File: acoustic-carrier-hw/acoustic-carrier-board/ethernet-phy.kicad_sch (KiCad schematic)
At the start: 52 parts, among them IC1 ECP5-BGA256, J12 HR911130A, U1 KSZ9031RN, Y1 25MHz

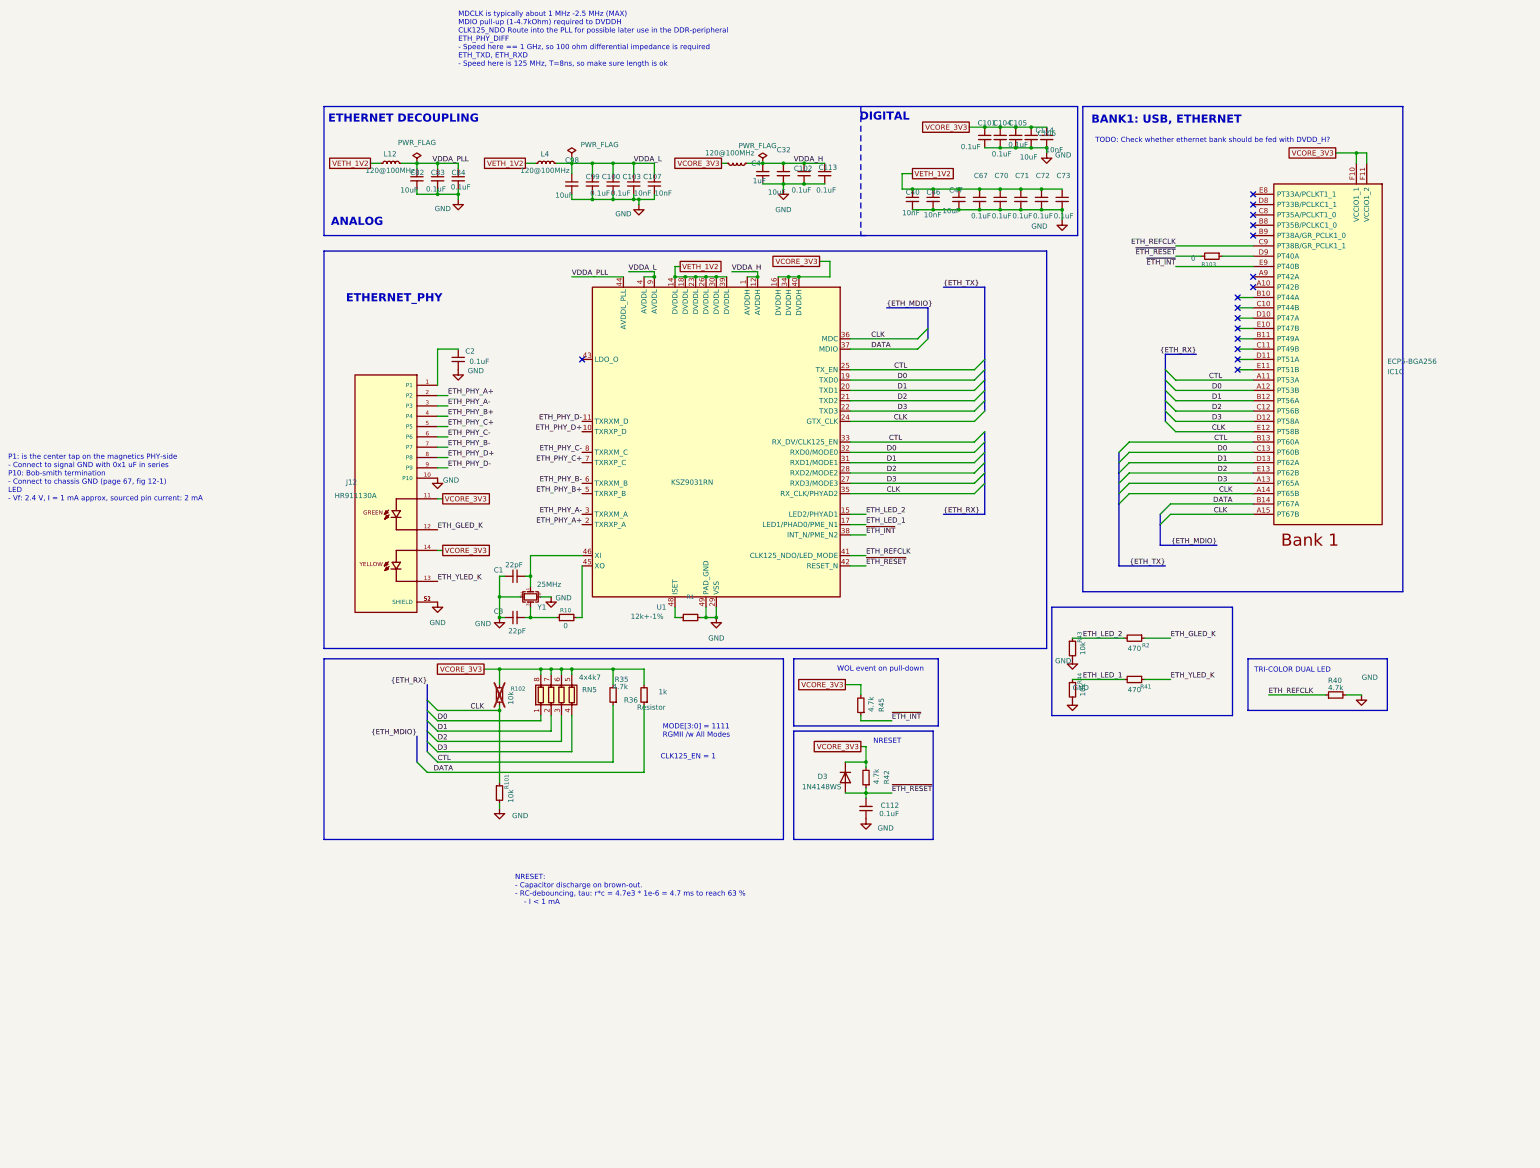
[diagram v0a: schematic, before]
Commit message: [carrier] Added hierarchical labels
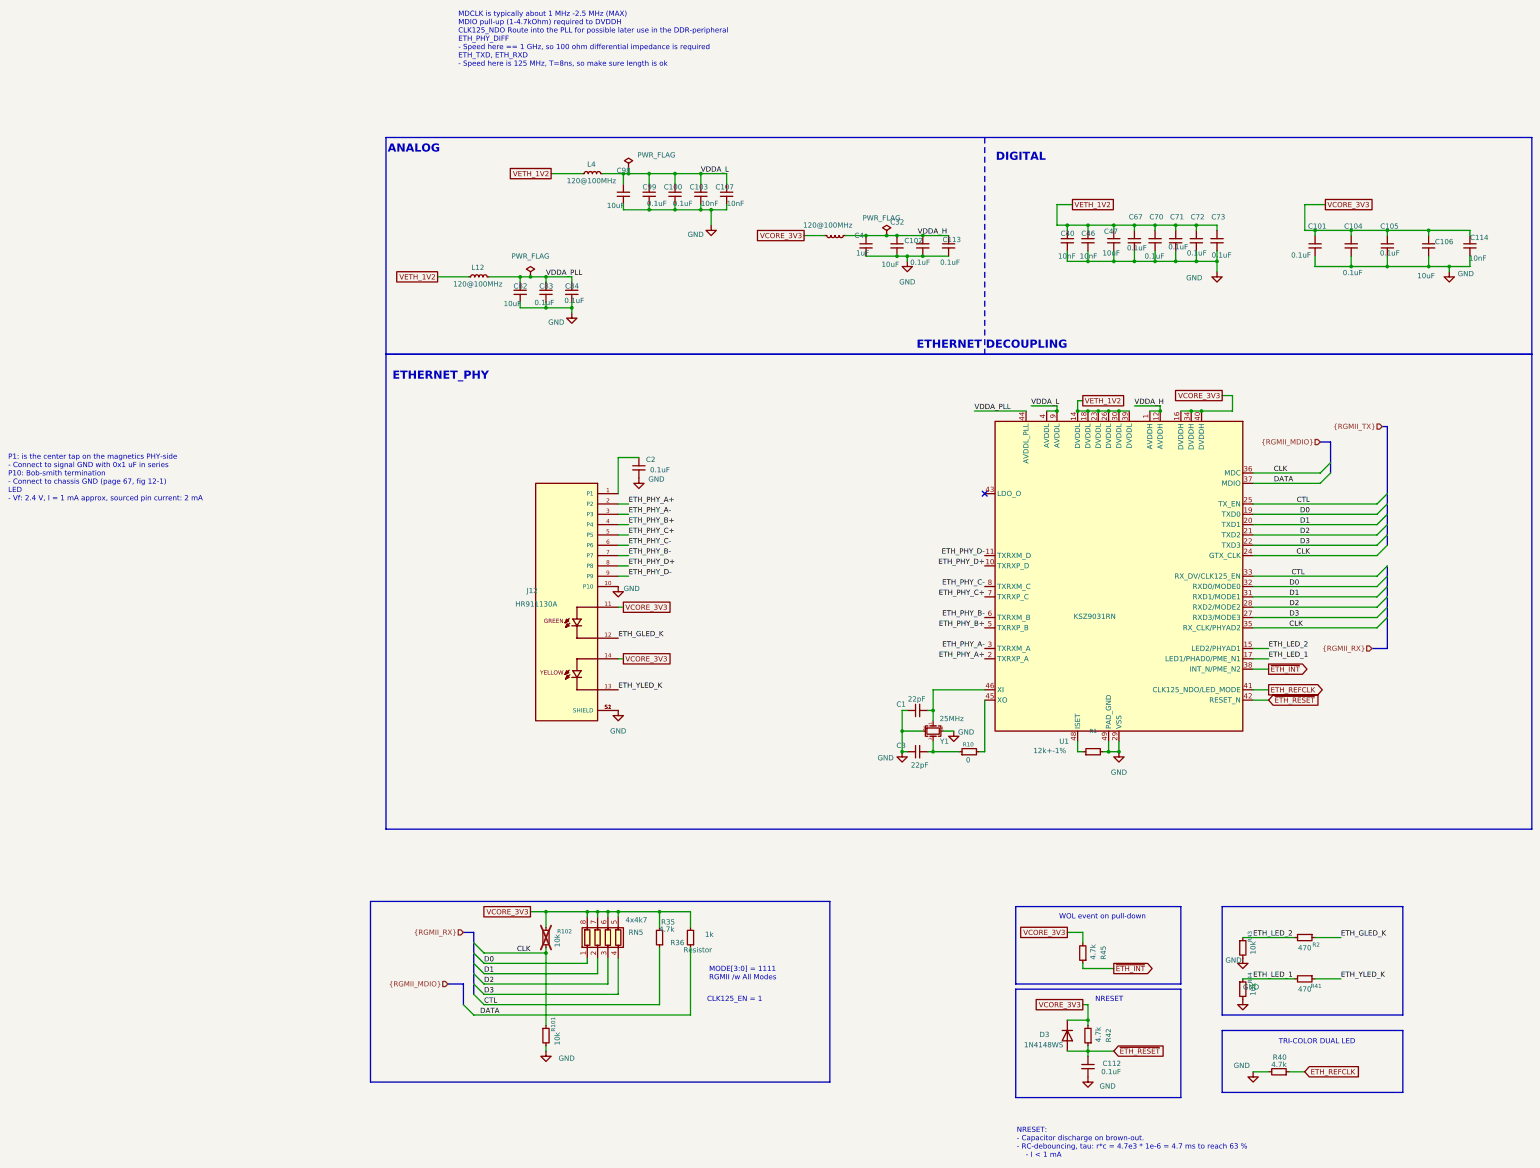
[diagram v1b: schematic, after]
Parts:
- removed IC1: ECP5-BGA256, iw-fpga_mcu:BGA256C80P16X16_1400X1400X170, symbol iw-fpga_mcu:ECP5-BGA256
- removed R103: 0, Resistor_SMD:R_0603_1608Metric, symbol Device:R_Small
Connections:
- no-connect marks 16 -> 1
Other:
- note removed: "BANK1: USB, ETHERNET"
- note removed: "TODO: Check whether ethernet bank should be fed with DVDD_H?"
- moved on the sheet: C1, C100, C101, C102, C103, C104, C105, C106, C107, C112, C113, C114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

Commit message: [¢arrier] Did major cchecks of ETH, DDR, ANALOG, config (next) check buffer circuit driven by USB-CC, then start layout
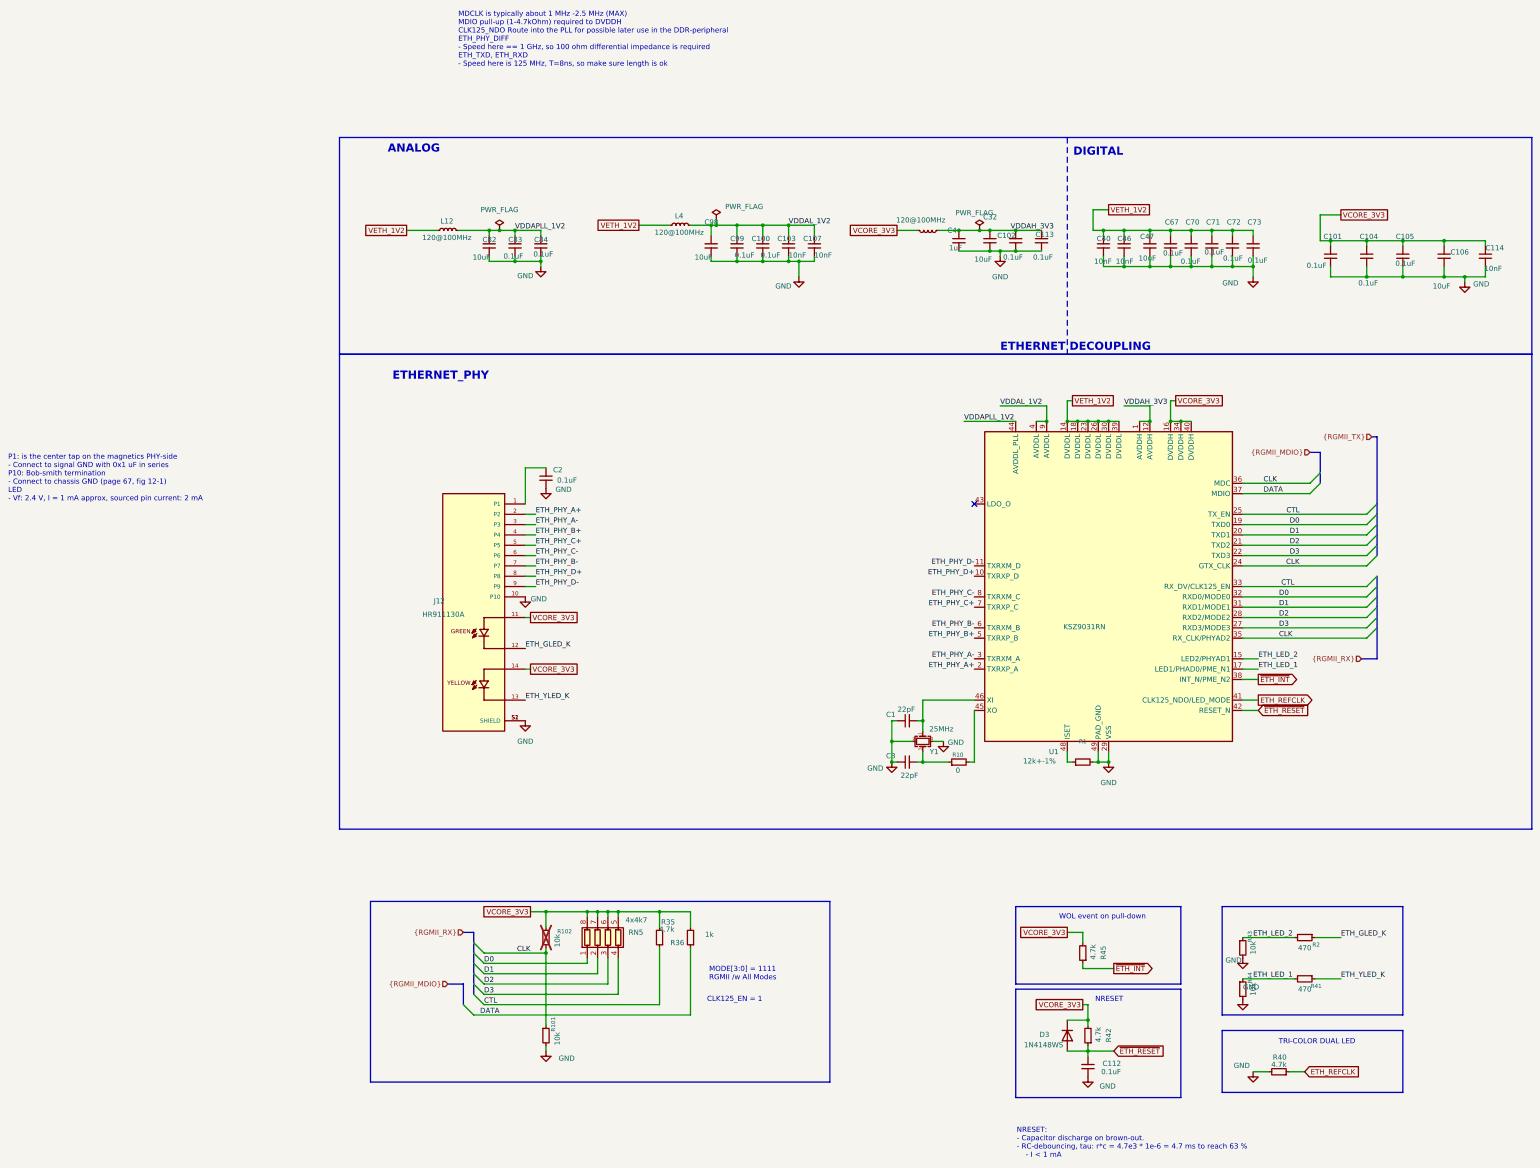
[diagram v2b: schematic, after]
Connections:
- net VDDA_H renamed VDDAH_3V3
- net VDDA_L renamed VDDAL_1V2
- net VDDA_PLL renamed VDDAPLL_1V2
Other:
- moved on the sheet: C1, C100, C101, C102, C103, C104, C105, C106, C107, C113, C114, C2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

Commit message: [carrier] Added testpoints
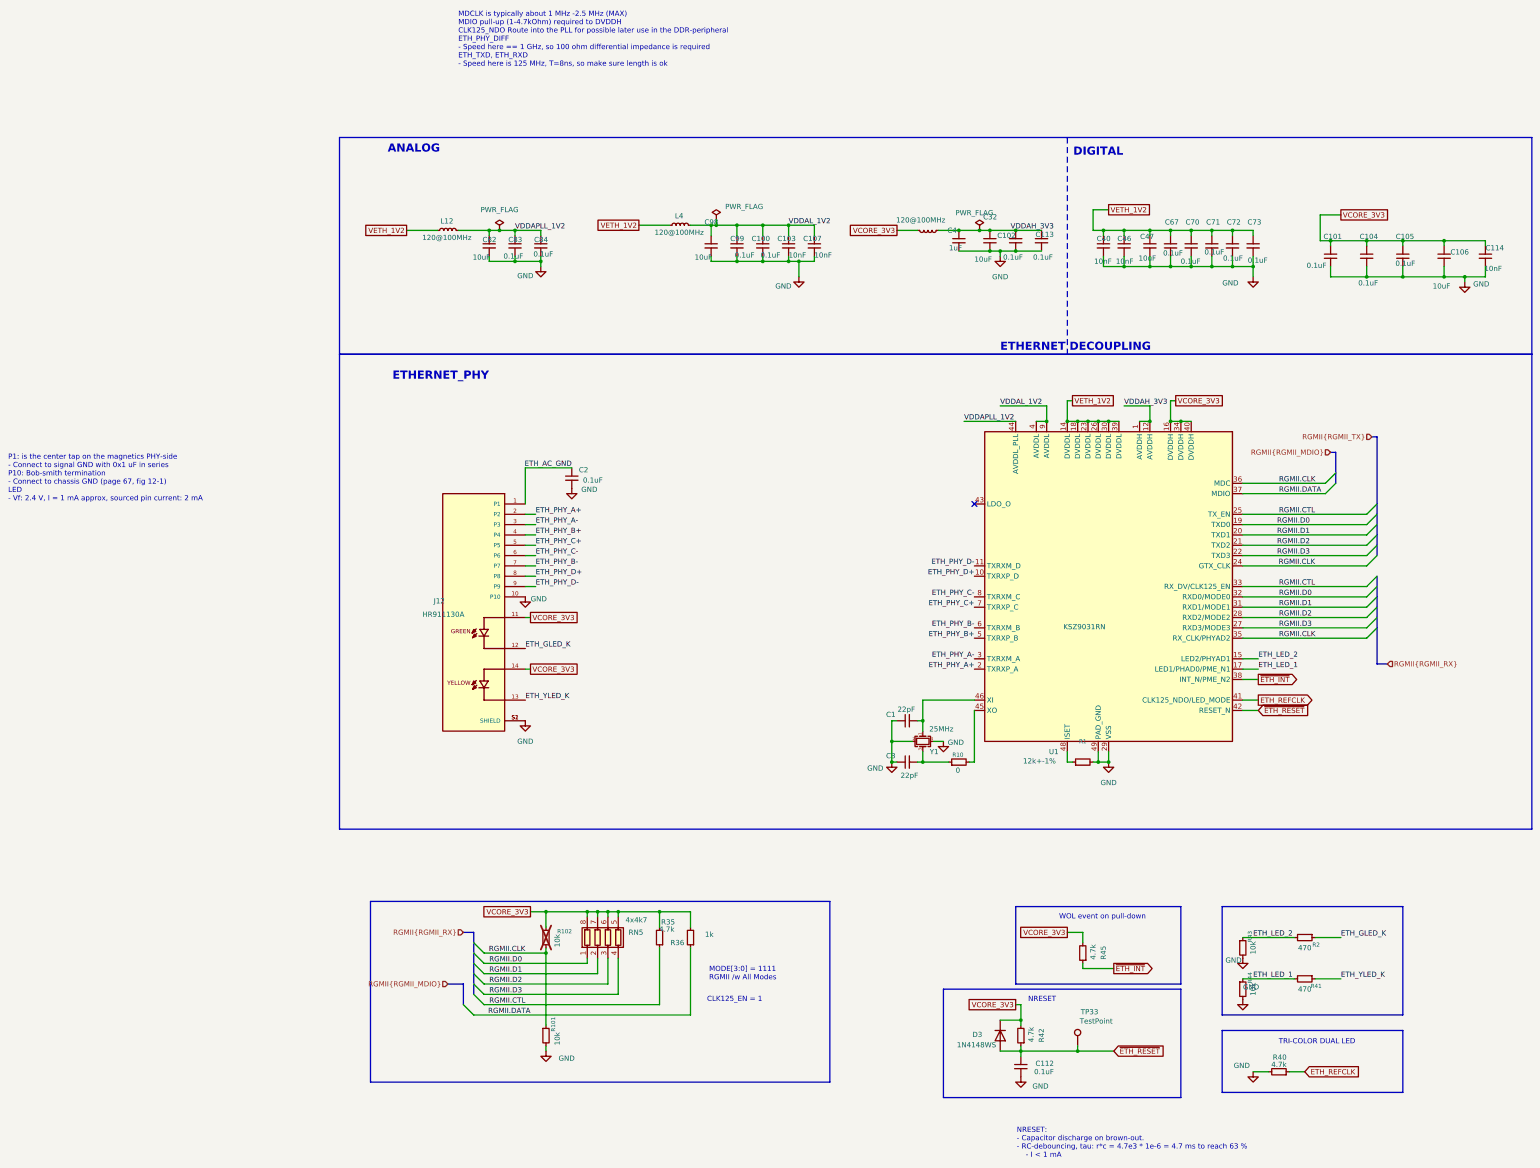
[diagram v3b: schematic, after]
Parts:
- added TP33: TestPoint, TestPoint:TestPoint_Loop_D1.80mm_Drill1.0mm_Beaded, symbol Connector:TestPoint
- R35, R40, R42, R45: LPN 0402WGF4701TCE -> C25900; MPN C25900 -> 0402WGF4701TCE
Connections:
- net ~{ETH_RESET}: now also TP33.1
- net ETH_AC_GND: now reaches C2.1, J12.1 (P1)
- net CLK renamed RGMII.CLK
- net CTL renamed RGMII.CTL
- net D0 renamed RGMII.D0
- net D1 renamed RGMII.D1
- net D2 renamed RGMII.D2
- net D3 renamed RGMII.D3
- net DATA renamed RGMII.DATA
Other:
- moved on the sheet: C112, C2, D3, R42

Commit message: [carrier] Finished rough layout, p (put together according to component category
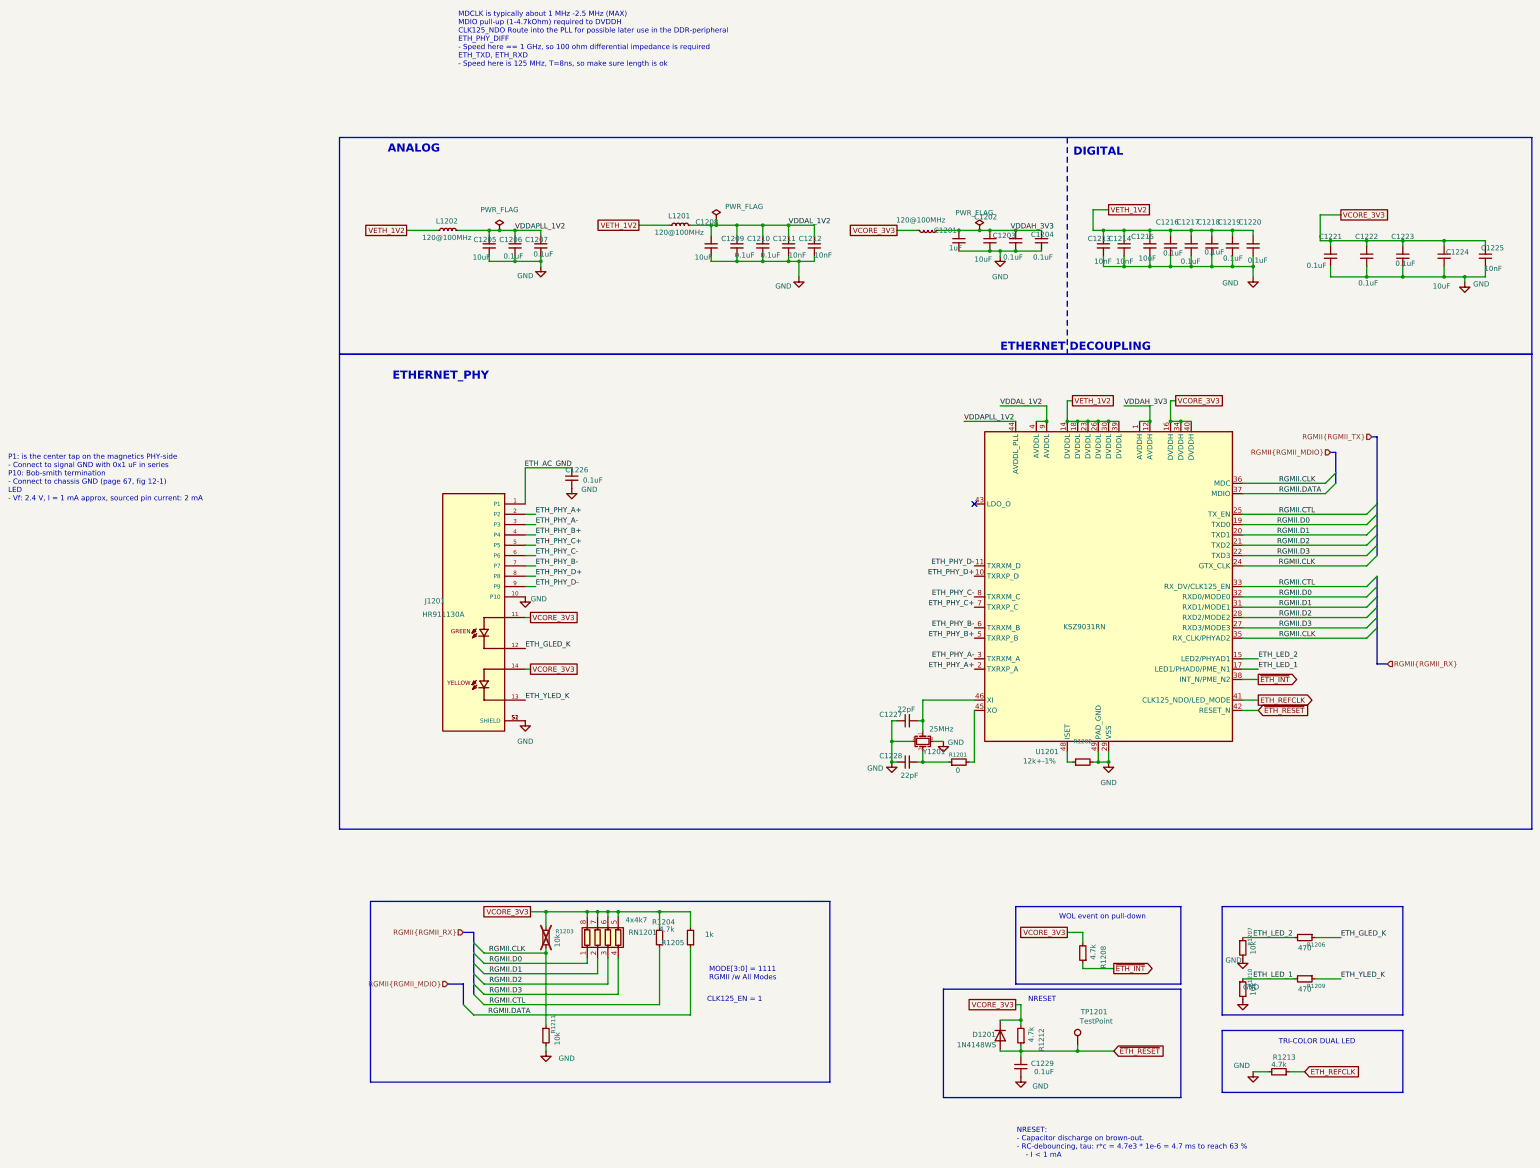
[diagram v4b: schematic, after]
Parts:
- renumbered C4 to C1201, C32 to C1202, C102 to C1203, C113 to C1204, C82 to C1205, C83 to C1206, C84 to C1207, C98 to C1208, C99 to C1209, C100 to C1210, C103 to C1211, C107 to C1212, C40 to C1213, C46 to C1214, C47 to C1215, C67 to C1216, C70 to C1217, C71 to C1218, C72 to C1219, C73 to C1220, C101 to C1221, C104 to C1222, C105 to C1223, C106 to C1224, C114 to C1225, C2 to C1226, C1 to C1227, C3 to C1228, C112 to C1229, D3 to D1201, J12 to J1201, L4 to L1201, L12 to L1202, L5 to L1203, R10 to R1201, R1 to R1202, R102 to R1203, R35 to R1204, R36 to R1205, R2 to R1206, R43 to R1207, R45 to R1208, R41 to R1209, R44 to R1210, R101 to R1211, R42 to R1212, R40 to R1213, RN5 to RN1201, TP33 to TP1201, U1 to U1201, Y1 to Y1201
